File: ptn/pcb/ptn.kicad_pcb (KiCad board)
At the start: 2 copper layers, 102 parts, among them IC1 ADP150AUJZ-3.3-R7, IC2 AZ1084CD-5.0TRG1, IC3 GRF5509, J1 TB002-500-04BE, J2 IO_BREAKOUT_CONN, J3 NRF_CONN, J4 Conn_01x04, J5 142-0701-801, J6 IO_CTRL_JP_BANK, SW1 SW_Push, U1 NCP1117-3.3_SOT223, U2 ADF4351, U3 MCP2551-I-SN, U4 STM32F103C8T6, Y1 SIT5000AICGE-33E0-25.000000X, Y2 16MHz

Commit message: Organize subsystem layouts
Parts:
- C55: footprint Capacitor_SMD:C_0603_1608Metric -> Capacitor_SMD:C_0402_1005Metric
- moved J3 162.6 mm to (167.7, 58.2)
- moved JP13 132.7 mm to (111.6, 53.8), turned to 90 degrees
- moved SW1 120.3 mm to (134.8, 55.0), turned to -90 degrees
- moved Y2 116.5 mm to (107.5, 67.8), turned to -90 degrees
- moved R16 114.4 mm to (115.1, 58.4), turned to 180 degrees
- moved J4 108.4 mm to (128.2, 53.8), turned to -90 degrees
- moved FB1 108.2 mm to (113.0, 73.2), turned to -90 degrees
- moved C57 107.1 mm to (110.2, 67.1), turned to -90 degrees
- moved C59 107.1 mm to (110.2, 69.0), turned to -90 degrees
- moved C39 105.8 mm to (108.2, 60.0)
- moved C41 104.9 mm to (112.4, 64.7), turned to -90 degrees
- moved C58 103.2 mm to (110.6, 74.4)
- moved C56 103.2 mm to (110.6, 72.1)
- moved C43 102.1 mm to (115.2, 62.3), turned to 180 degrees
- moved C55 101.5 mm to (112.3, 69.0), turned to -90 degrees
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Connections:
- J4 pad 2: SWCLK -> SWDIO
- J4 pad 3: SWDIO -> SWCLK

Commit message: PTN routing
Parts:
- added H1: MountingHole_Pad, MountingHole:MountingHole_4.3mm_M4_Pad, F.Cu at (80.0, 50.0)
- added H2: MountingHole_Pad, MountingHole:MountingHole_4.3mm_M4_Pad, F.Cu at (164.0, 50.0)
- added H3: MountingHole_Pad, MountingHole:MountingHole_4.3mm_M4_Pad, F.Cu at (80.0, 134.0)
- added H4: MountingHole_Pad, MountingHole:MountingHole_4.3mm_M4_Pad, F.Cu at (164.0, 134.0)
- added J7: MCP2551_JUMPER_BANK, Connector_PinHeader_2.54mm:PinHeader_2x02_P2.54mm_Vertical, F.Cu at (97.4, 48.7)
- added J8: ADF_JUMPER_BANK, Connector_PinHeader_2.54mm:PinHeader_2x07_P2.54mm_Vertical, F.Cu at (78.7, 109.4)
- added J9: POWER_OUT_CONN, Connector_PinHeader_2.54mm:PinHeader_1x04_P2.54mm_Vertical, F.Cu at (80.0, 96.5)
- J2: value IO_BREAKOUT_CONN -> ADC_IN_CONN; footprint Connector_PinHeader_2.54mm:PinHeader_2x12_P2.54mm_Vertical -> Connector_PinHeader_2.54mm:PinHeader_1x02_P2.54mm_Vertical
- J6: value IO_CTRL_JP_BANK -> NRF_JUMPER_BANK; footprint Connector_PinHeader_2.54mm:PinHeader_2x12_P2.54mm_Vertical -> Connector_PinHeader_2.54mm:PinHeader_2x06_P2.54mm_Vertical
- moved J2 114.9 mm to (164.0, 81.5), turned to 0 degrees
- moved J6 93.7 mm to (151.3, 60.8), turned to 0 degrees
- moved D2 41.2 mm to (109.6, 85.8)
- moved R5 41.2 mm to (112.6, 85.8)
- moved C2 39.8 mm to (116.8, 96.6), turned to 180 degrees
- moved IC1 39.4 mm to (116.3, 99.6), turned to -90 degrees
- moved R17 39.1 mm to (89.5, 72.0)
- moved R7 38.9 mm to (89.6, 75.7)
- moved U3 38.4 mm to (94.2, 71.9)
- moved C5 38.3 mm to (103.0, 79.8)
- moved IC2 38.3 mm to (111.0, 79.9)
- moved C10 37.1 mm to (109.0, 74.1)
- moved D1 36.7 mm to (94.2, 80.8)
- moved J1 34.9 mm to (80.0, 69.6)
- moved C9 34.1 mm to (116.9, 102.6), turned to 180 degrees
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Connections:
- J1 pad 1: /12V_IN -> CANL
- J1 pad 2: GND -> CANH
- J1 pad 3: CANL -> /12V_IN
- J1 pad 4: CANH -> GND
- J2 pad 1: +5V -> STM32_ADC1_IN0
- J2 pad 2: +3.3V -> GND
- J6 pad 1: STM32_SPI1_SCK -> NRF24L01P_IRQ
- J6 pad 10: STM32_NRF_CE -> NRF24L01P_MOSI
- J6 pad 11: STM32_CANTX -> NRF24L01P_CE
- J6 pad 12: STM32_CANRX -> NRF24L01P_IRQ
- J6 pad 2: STM32_SPI1_MOSI -> STM32_NRF_CE
- J6 pad 3: STM32_SPI1_SSN -> STM32_SPI2_MOSI
- J6 pad 4: STM32_ADF_CE -> STM32_SPI2_MISO
- J6 pad 5: STM32_ADF_PDBRF -> STM32_SPI2_SCK
- J6 pad 6: STM32_SPI2_SCK -> STM32_SPI2_SSN
- J6 pad 7: STM32_SPI2_MISO -> NRF24L01P_SSN
- J6 pad 8: STM32_SPI2_MOSI -> NRF24L01P_SCK
- J6 pad 9: STM32_SPI2_SSN -> NRF24L01P_MISO
- U3 pad 1: STM32_CANTX -> MCP2551_CANTX
- U3 pad 4: STM32_CANRX -> MCP2551_CANRX
- U4 pad 19: ADF4351_LD -> STM32_ADF_LD
- U4 pad 2: /STM32_USER_LED -> unconnected-(U4-PC13-Pad2)
- U4 pad 20: ADF4351_MUXOUT -> STM32_ADF_MUXOUT
- U4 pad 21: unconnected-(U4-PB10-Pad21) -> /STM32_USER_LED
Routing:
- net STM32_ADF_CE: track 0.00 -> 104.1 mm
- net STM32_SPI1_SSN: track 0.00 -> 101.0 mm
- net STM32_SPI1_MOSI: track 0.00 -> 98.9 mm
- net STM32_SPI1_SCK: track 0.00 -> 95.4 mm
- net STM32_ADF_MUXOUT: track 0.00 -> 92.0 mm
- net STM32_ADF_PDBRF: track 0.00 -> 89.8 mm
- net STM32_ADF_LD: track 0.00 -> 86.6 mm
- net +5V: track 0.00 -> 61.3 mm, vias 0 -> 4
- net STM32_ADC1_IN0: track 0.00 -> 48.2 mm
- net STM32_CANRX: track 0.00 -> 46.6 mm
- net STM32_CANTX: track 0.00 -> 39.9 mm
- net NRF24L01P_IRQ: track 0.00 -> 34.5 mm
- net GND: track 0.00 -> 28.1 mm, vias 0 -> 34
- net SWDIO: track 0.00 -> 27.9 mm
- net STM32_NRST: track 0.00 -> 27.7 mm
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- added copper zone on F.Cu, net +12V
- added copper zone on F.Cu, net +3.3V
- added copper zone on F.Cu, net +3.3VA
- added copper zone on F.Cu, net +5V
- added copper zone on B.Cu, net GND
- added copper zone on F.Cu, net GND
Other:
- board outline added: 100 x 100 mm

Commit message: PTN PCB Layout part 2
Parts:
- moved C2 22.1 mm to (96.3, 104.9)
- moved C9 22.1 mm to (96.4, 110.9)
- moved IC1 22.1 mm to (95.9, 107.9)
- moved FB1 3.12 mm to (119.0, 71.1)
- moved C56 1.58 mm to (121.3, 70.3), turned to 180 degrees
- moved C58 1.56 mm to (121.3, 71.8), turned to 180 degrees
- moved R14 0.39 mm to (153.0, 110.4)
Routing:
- net +3.3V: track 11.7 -> 168.4 mm, vias 0 -> 10
- net +5V: track 61.3 -> 213.6 mm
- net GND: track 28.1 -> 30.1 mm, vias 34 -> 36

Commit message: PTN routing part 3
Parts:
- removed the L4 at (123.8, 117.5)
- R3: renamed from R2; footprint Resistor_SMD:R_0603_1608Metric -> Resistor_SMD:R_0402_1005Metric
- moved C27 43.4 mm to (142.6, 135.8)
- moved C24 43.4 mm to (142.5, 134.4)
- moved C26 12.0 mm to (136.2, 119.2), turned to -90 degrees
- moved C32 11.6 mm to (128.8, 112.5)
- moved C31 11.6 mm to (128.8, 111.5)
- moved C22 11.6 mm to (126.7, 118.3)
- moved C19 11.5 mm to (127.7, 118.3)
- moved C11 11.3 mm to (135.0, 113.3)
- moved C13 11.3 mm to (136.0, 113.3)
- moved C25 11.3 mm to (129.3, 110.3)
- moved C28 11.3 mm to (129.3, 109.3)
- moved R9 11.3 mm to (112.3, 117.3)
- moved U3 11.3 mm to (131.4, 116.3)
- moved Y1 11.3 mm to (116.3, 117.3)
- moved C12 11.3 mm to (116.0, 114.5)
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- renumbered J3 to J2, J6 to J3, J2 to J4, J9 to J5, J7 to J6, J8 to J7, J4 to J8, J5 to J9, JP13 to JP1, L1 to L2, L2 to L3, L3 to L4, R7 to R1, R9 to R10, R10 to R11, R11 to R12, R12 to R13, R13 to R14, R14 to R15, R15 to R16, R16 to R17, R1 to R2, R3 to R4, R4 to R5, R17 to R6, R5 to R7, R6 to R8, R8 to R9, U3 to U1, U1 to U2, U2 to U3
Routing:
- net +3.3VA: track 5.26 -> 219.5 mm, vias 0 -> 8
- net +3.3V: track 168.4 -> 228.0 mm, vias 10 -> 18
- net ADF4351_CE: track 0.00 -> 55.0 mm
- net ADF4351_SSN: track 0.00 -> 54.9 mm
- net ADF4351_MOSI: track 0.00 -> 54.7 mm
- net ADF4351_SCK: track 0.00 -> 54.6 mm
- net ADF4351_MUXOUT: track 0.00 -> 53.9 mm
- net GND: track 30.1 -> 83.1 mm, vias 36 -> 121
- net ADF4351_LD: track 0.00 -> 49.9 mm
- net ADF4351_PDBRF: track 0.00 -> 49.1 mm
- net ADF4351_CPOUT: track 0.00 -> 20.8 mm, vias 0 -> 2
- net Net-(IC3-RF_OUT/VCC2_1): track 0.00 -> 9.12 mm
- net /GRF5509_RFOUT: track 0.00 -> 7.07 mm
- net ADF4351_VTUNE: track 0.00 -> 6.24 mm
- net +5V: track 213.6 -> 208.2 mm
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
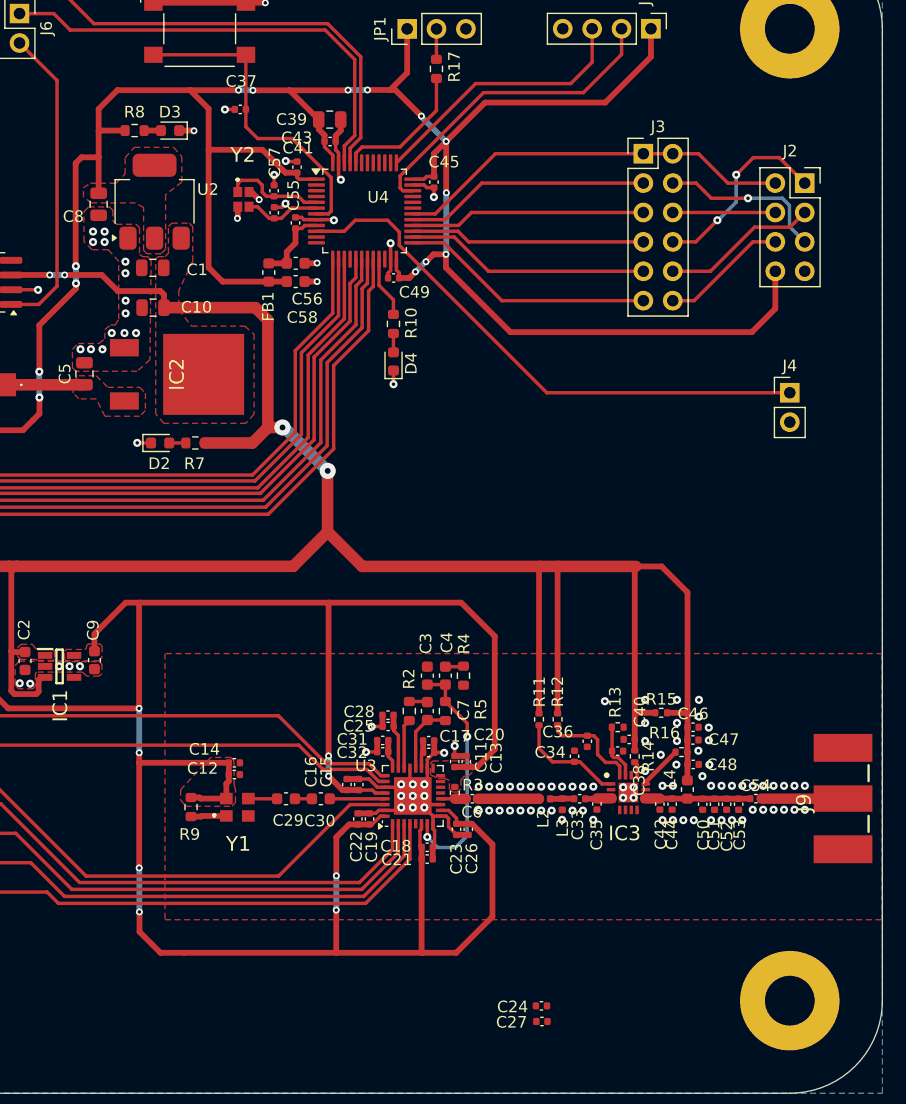
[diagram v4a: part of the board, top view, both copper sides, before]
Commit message: finish all routing for ptn
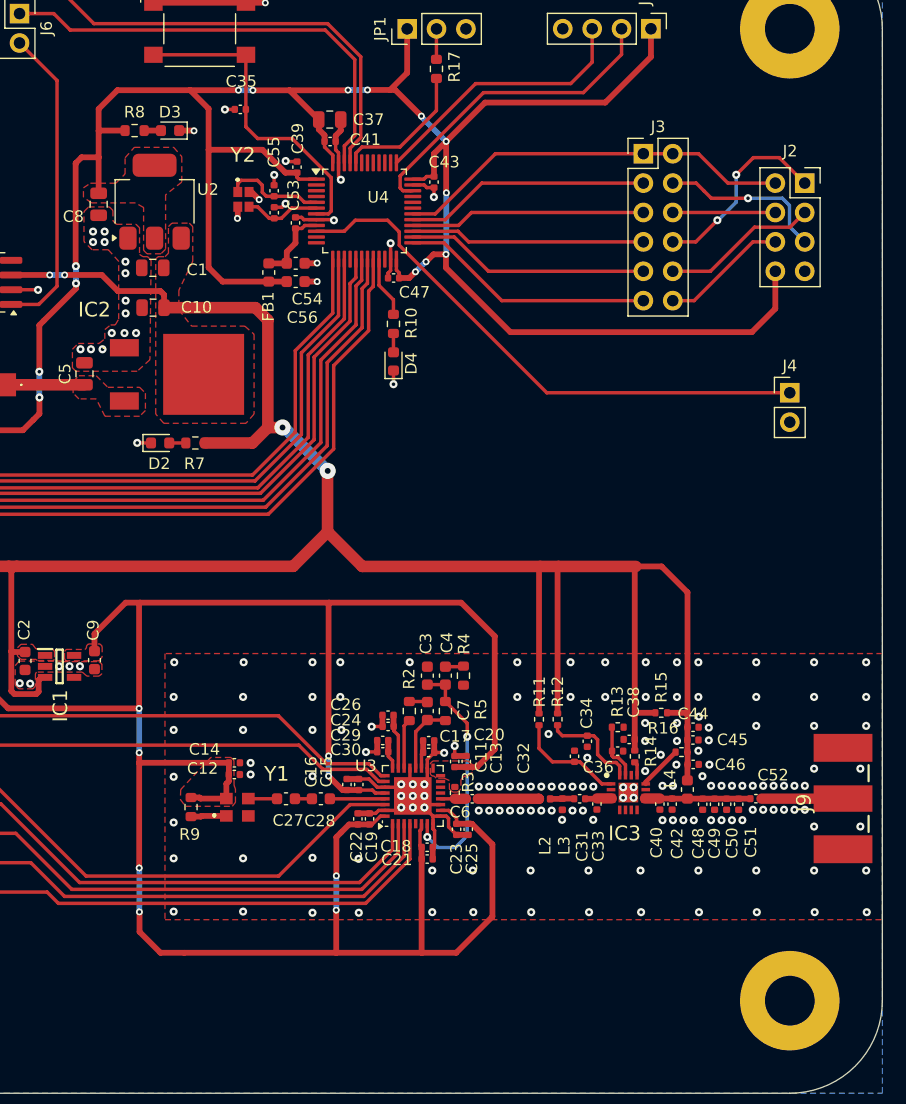
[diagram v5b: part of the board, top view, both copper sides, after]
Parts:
- removed the C24 at (142.5, 134.4)
- removed the C27 at (142.6, 135.8)
- renumbered C25 to C24, C26 to C25, C28 to C26, C29 to C27, C30 to C28, C31 to C29, C32 to C30, C33 to C31, C34 to C32, C35 to C33, C36 to C34, C37 to C35, C38 to C36, C39 to C37, C40 to C38, C41 to C39, C42 to C40, C43 to C41, C44 to C42, C45 to C43, C46 to C44, C47 to C45, C48 to C46, C49 to C47, C50 to C48, C51 to C49, C52 to C50, C53 to C51, C54 to C52, C55 to C53, C56 to C54, C57 to C55, C58 to C56, C59 to C57
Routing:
- net GND: vias 121 -> 188

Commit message: complete layout pending review
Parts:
- added J7: UART_CONN, Connector_PinHeader_2.54mm:PinHeader_1x02_P2.54mm_Vertical, F.Cu at (164.0, 91.5)
- moved D4 25.4 mm to (145.9, 59.1), turned to 180 degrees
- moved R11 20.9 mm to (142.7, 59.1), turned to 180 degrees
- moved C47 0.38 mm to (130.1, 71.5)
- renumbered J9 to J10, J7 to J8, J8 to J9, R11 to R10, R10 to R11
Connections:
- U4 pad 21: /STM32_USER_LED -> STM32_USART3_TX
- U4 pad 22: unconnected-(U4-PB11-Pad22) -> STM32_USART3_RX
- U4 pad 31: unconnected-(U4-PA10-Pad31) -> /STM32_USER_LED
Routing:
- net STM32_USART3_TX: track 0.00 -> 51.0 mm
- net STM32_USART3_RX: track 0.00 -> 49.3 mm
- net /STM32_USER_LED: track 5.29 -> 13.1 mm

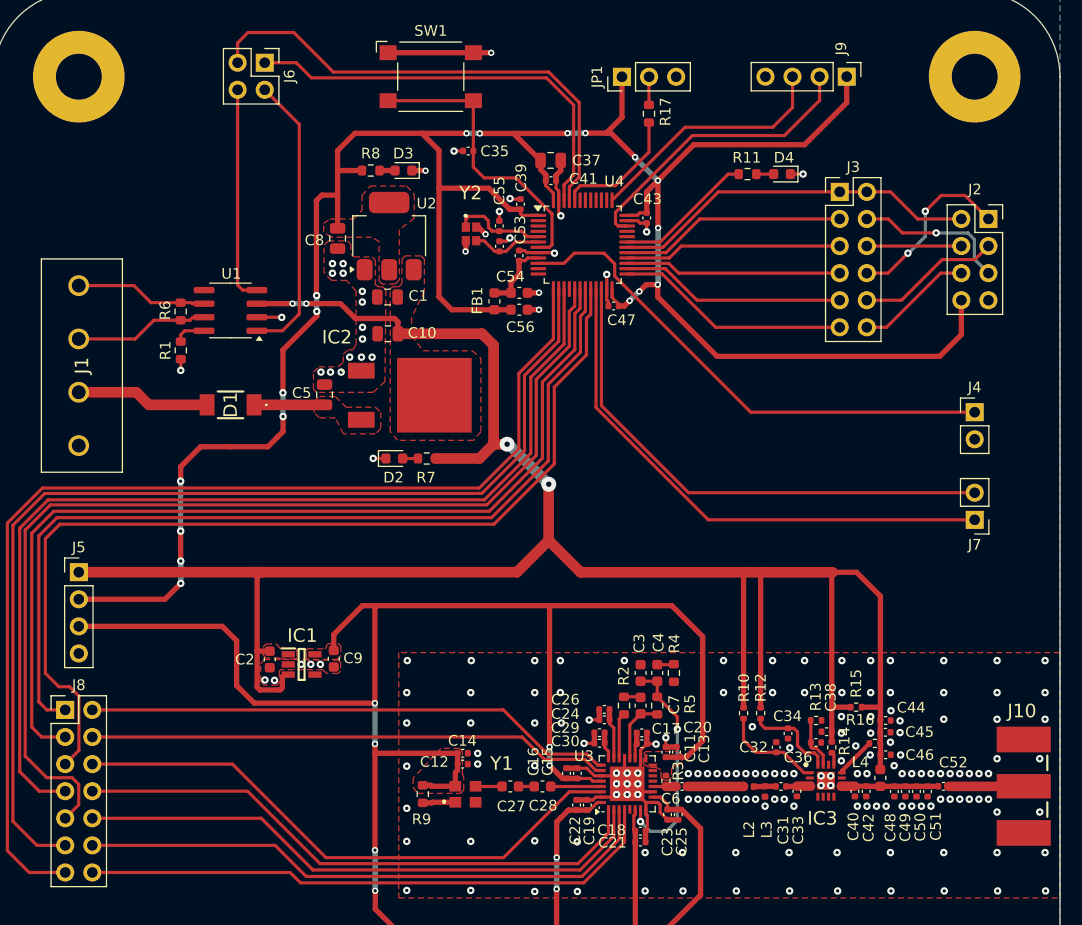
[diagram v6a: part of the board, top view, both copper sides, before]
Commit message: Add another ADP150 LDO, improve T-line
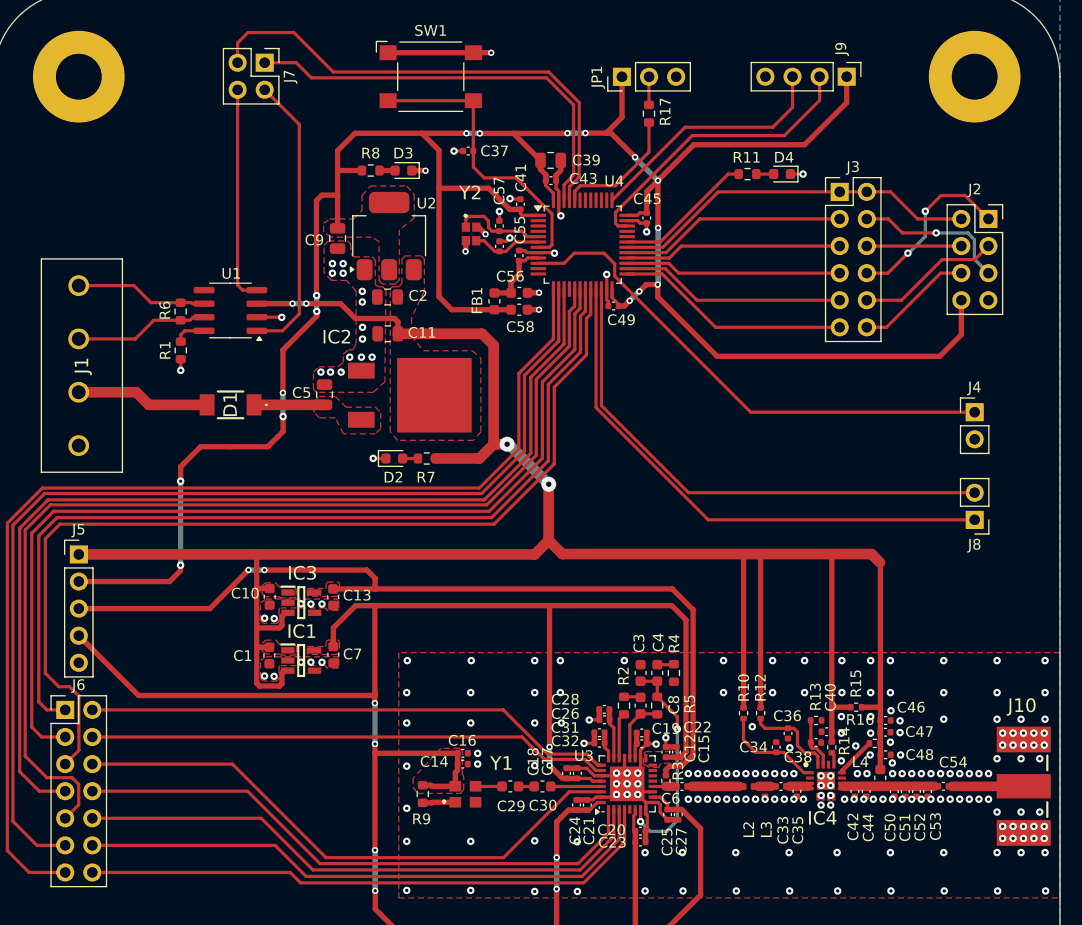
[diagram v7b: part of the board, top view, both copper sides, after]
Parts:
- added C10: 1u, Capacitor_SMD:C_0603_1608Metric, F.Cu at (97.9, 98.8)
- added C13: 1u, Capacitor_SMD:C_0603_1608Metric, F.Cu at (103.9, 98.8)
- added IC3: ADP150AUJZ-3.3-R7, project_footprint_library:SOT95P280X100-5N, F.Cu at (100.9, 99.3)
- J5: footprint Connector_PinHeader_2.54mm:PinHeader_1x04_P2.54mm_Vertical -> Connector_PinHeader_2.54mm:PinHeader_1x05_P2.54mm_Vertical
- moved J5 1.66 mm to (80.0, 94.8)
- moved C1 0.37 mm to (97.9, 104.3)
- moved C7 0.37 mm to (103.9, 104.2)
- moved IC1 0.37 mm to (100.8, 104.7)
- renumbered C2 to C1, C10 to C11, C11 to C12, C12 to C14, C13 to C15, C14 to C16, C15 to C17, C16 to C18, C17 to C19, C1 to C2, C18 to C20, C19 to C21, C20 to C22, C21 to C23, C22 to C24, C23 to C25, C24 to C26, C25 to C27, C26 to C28, C27 to C29, C28 to C30, C29 to C31, C30 to C32, C31 to C33, C32 to C34, C33 to C35, C34 to C36, C35 to C37, C36 to C38, C37 to C39, C38 to C40, C39 to C41, C40 to C42, C41 to C43, C42 to C44, C43 to C45, C44 to C46, C45 to C47, C46 to C48, C47 to C49, C48 to C50, C49 to C51, C50 to C52, C51 to C53, C52 to C54, C53 to C55, C54 to C56, C55 to C57, C56 to C58, C57 to C59, C9 to C7, C7 to C8, C8 to C9, IC3 to IC4, J8 to J6, J6 to J7, J7 to J8
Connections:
- J5 pad 3: +3.3VA -> +3.3VA_VOUT
- J5 pad 4: GND -> +3.3VA
- R3 pad 1: +3.3VA -> +3.3VA_VOUT
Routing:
- net +3.3VA_VOUT: track 0.00 -> 82.4 mm, vias 0 -> 2
- net +5V: track 208.2 -> 220.3 mm
- net +3.3VA: track 219.5 -> 214.8 mm
- net +3.3V: track 227.7 -> 226.3 mm, vias 18 -> 16
- net Net-(C33-Pad1): track 2.08 -> 1.20 mm
- net GRF5509_RFIN: track 5.29 -> 4.44 mm
- net Net-(IC4-RF_IN_1): track 2.31 -> 1.76 mm
- net Net-(IC4-RF_OUT/VCC2_1): track 9.12 -> 8.59 mm
- net GND: vias 188 -> 225
- added copper zone on F.Cu, net +3.3VA_VOUT

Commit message: Layout review and optimization
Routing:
- net GND: track 83.0 -> 92.9 mm, vias 225 -> 227
